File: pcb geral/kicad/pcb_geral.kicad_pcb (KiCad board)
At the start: 2 copper layers, 138 x 57 mm, 6 parts

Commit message: Another Day
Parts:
- removed KeyboardPinSocket: PinSocket_2x07_P2.54mm_Vertical, Connector_PinSocket_2.54mm:PinSocket_2x07_P2.54mm_Vertical
- added KeyboardSocket_1: PinSocket_1x07_P2.54mm_Vertical, Connector_PinSocket_2.54mm:PinSocket_1x07_P2.54mm_Vertical, F.Cu at (84.7, 122.5)
- added KeyboardSocket_2: PinSocket_1x07_P2.54mm_Vertical, Connector_PinSocket_2.54mm:PinSocket_1x07_P2.54mm_Vertical, F.Cu at (84.6, 126.1)
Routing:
- net (no net): track 1061.2 -> 848.6 mm
- net .: track 1561.3 -> 1769.5 mm

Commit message: Another Day
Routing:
- net (no net): track 848.6 -> 854.1 mm
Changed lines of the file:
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@@
+	)
+	(segment
+		(start 96.75 85.65)
+		(end 96.6 85.8)
+		(width 0.1)
+		(layer "F.Cu")
+		(net 0)
 	)
 	(segment
@@
 	)
 	(segment
+		(start 96.6 85.8)
+		(end 96.6 87.3)
+		(width 0.1)
+		(layer "F.Cu")
+		(net 0)
+	)
+	(segment
 		(start 95.45 78.25)
 		(end 96.95 76.75)
@@
 	)
 	(segment
+		(start 95.25 88.65)
+		(end 95.25 89.1)
+		(width 0.1)
+		(layer "F.Cu")
+		(net 0)
+	)
+	(segment
+		(start 96.6 87.3)
+		(end 95.25 88.65)
+		(width 0.1)
+		(layer "F.Cu")
+		(net 0)
+	)
+	(segment
 		(start 163.663894 83.336106)
 		(end 162.75 84.25)
@@
 		(start 98.75 86.7)
 		(end 98.75 84.2)
+		(width 0.1)
+		(layer "F.Cu")
+		(net 0)
+	)
+	(segment
+		(start 96.75 84.2)
+		(end 96.75 85.65)
 		(width 0.1)
 		(layer "F.Cu")
@@
 	)
 	(segment
+		(start 97 86.65)
+		(end 97 87.4)
+		(width 0.1)
+		(layer "F.Cu")
+		(net 1)
+	)
+	(segment
 		(start 208 101.25)
 		(end 208.52 101.77)
@@
 	)
 	(segment
+		(start 97.25 86.4)
+		(end 97 86.65)
+		(width 0.1)
+		(layer "F.Cu")
+		(net 1)
+	)
+	(segment
 		(start 97.7 84.45)
 		(end 97.7 87.05)
@@
 	)
 	(segment
-		(start 96.25 87.4)
-		(end 96.25 89.1)
-		(width 0.1)
-		(layer "F.Cu")
-		(net 1)
-	)
-	(segment
 		(start 167.75 118.5)
 		(end 173 113.25)
@@
 	)
 	(segment
+		(start 97.2 119.8)
+		(end 97.25 119.75)
+		(width 0.6)
+		(layer "F.Cu")
+		(net 1)
+	)
+	(segment
+		(start 89.7 126)
+		(end 89.58 126.12)
+		(width 0.6)
+		(layer "F.Cu")
+		(net 1)
+	)
+	(segment
+		(start 155.25 101.25)
+		(end 208 101.25)
+		(width 0.6)
+		(layer "F.Cu")
+		(net 1)
+	)
+	(segment
+		(start 176.348843 113.551157)
+		(end 178.05 111.85)
+		(width 0.6)
+		(layer "F.Cu")
+		(net 1)
+	)
+	(segment
+		(start 84.5 126.2)
+		(end 84.5 132.199)
+		(width 0.6)
+		(layer "F.Cu")
+		(net 1)
+	)
+	(segment
+		(start 166.75 116.75)
+		(end 170.42 113.08)
+		(width 0.6)
+		(layer "F.Cu")
+		(net 1)
+	)
+	(segment
+		(start 176.348843 113.65099)
+		(end 176.348843 113.551157)
+		(width 0.6)
+		(layer "F.Cu")
+		(net 1)
+	)
+	(segment
+		(start 172.96 113.21)
+		(end 172.96 109.75)
+		(width 0.6)
+		(layer "F.Cu")
+		(net 1)
+	)
+	(segment
+		(start 94.66 127.66)
+		(end 94.75 127.75)
+		(width 0.6)
+		(layer "F.Cu")
+		(net 1)
+	)
+	(segment
+		(start 101.49 121)
+		(end 170.5 121)
+		(width 0.6)
+		(layer "F.Cu")
+		(net 1)
+	)
+	(segment
+		(start 89.58 122.75)
+		(end 89.58 115.42)
+		(width 0.6)
+		(layer "F.Cu")
+		(net 1)
+	)
+	(segment
+		(start 84.5 132.199)
+		(end 185.551 132.199)
+		(width 0.6)
+		(layer "F.Cu")
+		(net 1)
+	)
+	(segment
+		(start 94.66 122.75)
+		(end 94.66 118.59)
+		(width 0.6)
+		(layer "F.Cu")
+		(net 1)
+	)
+	(segment
+		(start 84.5 122.75)
+		(end 84.5 113)
+		(width 0.6)
+		(layer "F.Cu")
+		(net 1)
+	)
+	(segment
+		(start 178.05 111.85)
+		(end 178.05 111.6)
+		(width 0.6)
+		(layer "F.Cu")
+		(net 1)
+	)
+	(segment
+		(start 96.25 88.15)
+		(end 96.25 89.1)
+		(width 0.1)
+		(layer "F.Cu")
+		(net 1)
+	)
+	(segment
+		(start 94.66 118.59)
+		(end 94.75 118.5)
+		(width 0.6)
+		(layer "F.Cu")
+		(net 1)
+	)
+	(segment
+		(start 170.5 121)
+		(end 175.25 116.25)
+		(width 0.6)
+		(layer "F.Cu")
+		(net 1)
+	)
+	(segment
+		(start 94.75 127.75)
+		(end 176 127.75)
+		(width 0.6)
+		(layer "F.Cu")
+		(net 1)
+	)
+	(segment
+		(start 92.12 116.88)
+		(end 92.25 116.75)
+		(width 0.6)
+		(layer "F.Cu")
+		(net 1)
+	)
+	(segment
+		(start 189.25 110.8)
+		(end 188.2 109.75)
+		(width 0.6)
+		(layer "F.Cu")
+		(net 1)
+	)
+	(segment
+		(start 89.58 115.42)
+		(end 89.75 115.25)
+		(width 0.6)
+		(layer "F.Cu")
+		(net 1)
+	)
+	(segment
+		(start 189.25 121.25)
+		(end 189.25 110.8)
+		(width 0.6)
+		(layer "F.Cu")
+		(net 1)
+	)
+	(segment
 		(start 97.25 84.55)
 		(end 97.25 86.4)
 		(width 0.1)
-		(layer "F.Cu")
-		(net 1)
-	)
-	(segment
-		(start 97.2 119.8)
-		(end 97.25 119.75)
-		(width 0.6)
-		(layer "F.Cu")
-		(net 1)
-	)
-	(segment
-		(start 89.7 126)
-		(end 89.58 126.12)
-		(width 0.6)
-		(layer "F.Cu")
-		(net 1)
-	)
-	(segment
-		(start 155.25 101.25)
-		(end 208 101.25)
-		(width 0.6)
-		(layer "F.Cu")
-		(net 1)
-	)
-	(segment
-		(start 176.348843 113.551157)
-		(end 178.05 111.85)
-		(width 0.6)
-		(layer "F.Cu")
-		(net 1)
-	)
-	(segment
-		(start 84.5 126.2)
-		(end 84.5 132.199)
-		(width 0.6)
-		(layer "F.Cu")
-		(net 1)
-	)
-	(segment
-		(start 166.75 116.75)
-		(end 170.42 113.08)
-		(width 0.6)
-		(layer "F.Cu")
-		(net 1)
-	)
-	(segment
-		(start 176.348843 113.65099)
-		(end 176.348843 113.551157)
-		(width 0.6)
-		(layer "F.Cu")
-		(net 1)
-	)
-	(segment
-		(start 172.96 113.21)
-		(end 172.96 109.75)
-		(width 0.6)
-		(layer "F.Cu")
-		(net 1)
-	)
-	(segment
-		(start 94.66 127.66)
-		(end 94.75 127.75)
-		(width 0.6)
-		(layer "F.Cu")
-		(net 1)
-	)
-	(segment
-		(start 101.49 121)
-		(end 170.5 121)
-		(width 0.6)
-		(layer "F.Cu")
-		(net 1)
-	)
-	(segment
-		(start 89.58 122.75)
-		(end 89.58 115.42)
-		(width 0.6)
-		(layer "F.Cu")
-		(net 1)
-	)
-	(segment
-		(start 84.5 132.199)
-		(end 185.551 132.199)
-		(width 0.6)
-		(layer "F.Cu")
-		(net 1)
-	)
-	(segment
-		(start 94.66 122.75)
-		(end 94.66 118.59)
-		(width 0.6)
-		(layer "F.Cu")
-		(net 1)
-	)
-	(segment
-		(start 84.5 122.75)
-		(end 84.5 113)
-		(width 0.6)
-		(layer "F.Cu")
-		(net 1)
-	)
-	(segment
-		(start 178.05 111.85)
-		(end 178.05 111.6)
-		(width 0.6)
-		(layer "F.Cu")
-		(net 1)
-	)
-	(segment
-		(start 94.66 118.59)
-		(end 94.75 118.5)
-		(width 0.6)
-		(layer "F.Cu")
-		(net 1)
-	)
-	(segment
-		(start 170.5 121)
-		(end 175.25 116.25)
-		(width 0.6)
-		(layer "F.Cu")
-		(net 1)
-	)
-	(segment
-		(start 97.25 86.4)
-		(end 96.25 87.4)
-		(width 0.1)
-		(layer "F.Cu")
-		(net 1)
-	)
-	(segment
-		(start 94.75 127.75)
-		(end 176 127.75)
-		(width 0.6)
-		(layer "F.Cu")
-		(net 1)
-	)
-	(segment
-		(start 92.12 116.88)
-		(end 92.25 116.75)
-		(width 0.6)
-		(layer "F.Cu")
-		(net 1)
-	)
-	(segment
-		(start 189.25 110.8)
-		(end 188.2 109.75)
-		(width 0.6)
-		(layer "F.Cu")
-		(net 1)
-	)
-	(segment
-		(start 89.58 115.42)
-		(end 89.75 115.25)
-		(width 0.6)
-		(layer "F.Cu")
-		(net 1)
-	)
-	(segment
-		(start 189.25 121.25)
-		(end 189.25 110.8)
-		(width 0.6)
 		(layer "F.Cu")
 		(net 1)
@@
 		(layer "F.Cu")
 		(net 1)
+	)
+	(segment
+		(start 97 87.4)
+		(end 96.25 88.15)
+		(width 0.1)
+		(layer "F.Cu")
+		(net 1)

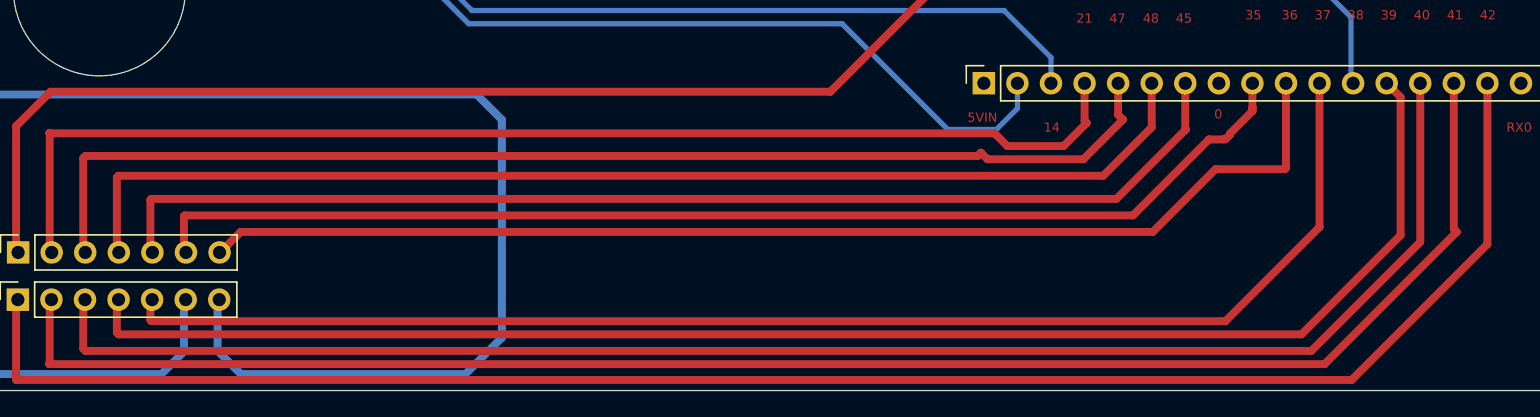
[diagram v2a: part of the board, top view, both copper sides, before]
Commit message: Added Battery Holder to BOM and modified PCB schematic
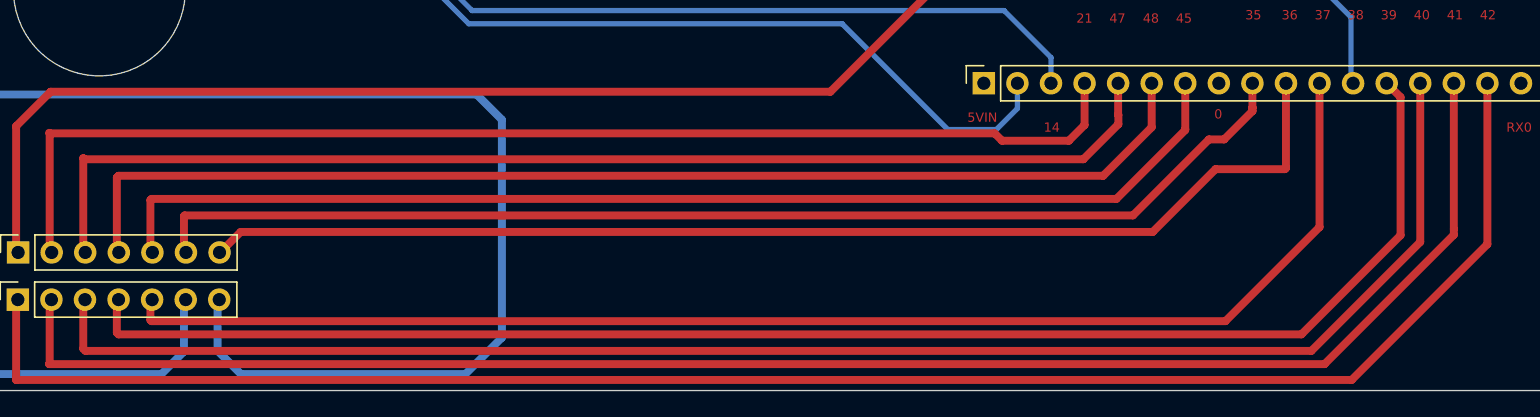
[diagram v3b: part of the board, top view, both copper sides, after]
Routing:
- net .: track 1769.5 -> 1768.1 mm

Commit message: Updated cart and schematics
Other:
- board text added: "ESP32"
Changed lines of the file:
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@@
+		)
+	)
+	(gr_text "ESP32"
+		(at 178.5 97.5 0)
+		(layer "F.Cu")
+		(effects
+			(font
+				(size 1.5 1.5)
+				(thickness 0.3)
+				(bold yes)
+			)
+			(justify left bottom)
 		)
 	)
